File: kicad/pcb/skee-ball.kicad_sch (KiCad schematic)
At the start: 6 parts, among them U1 D24V22F6, U2 MAX98357A, U3 D24V22F5, U4 STM32F091RCTx, U5 74HC595, U6 74HC595

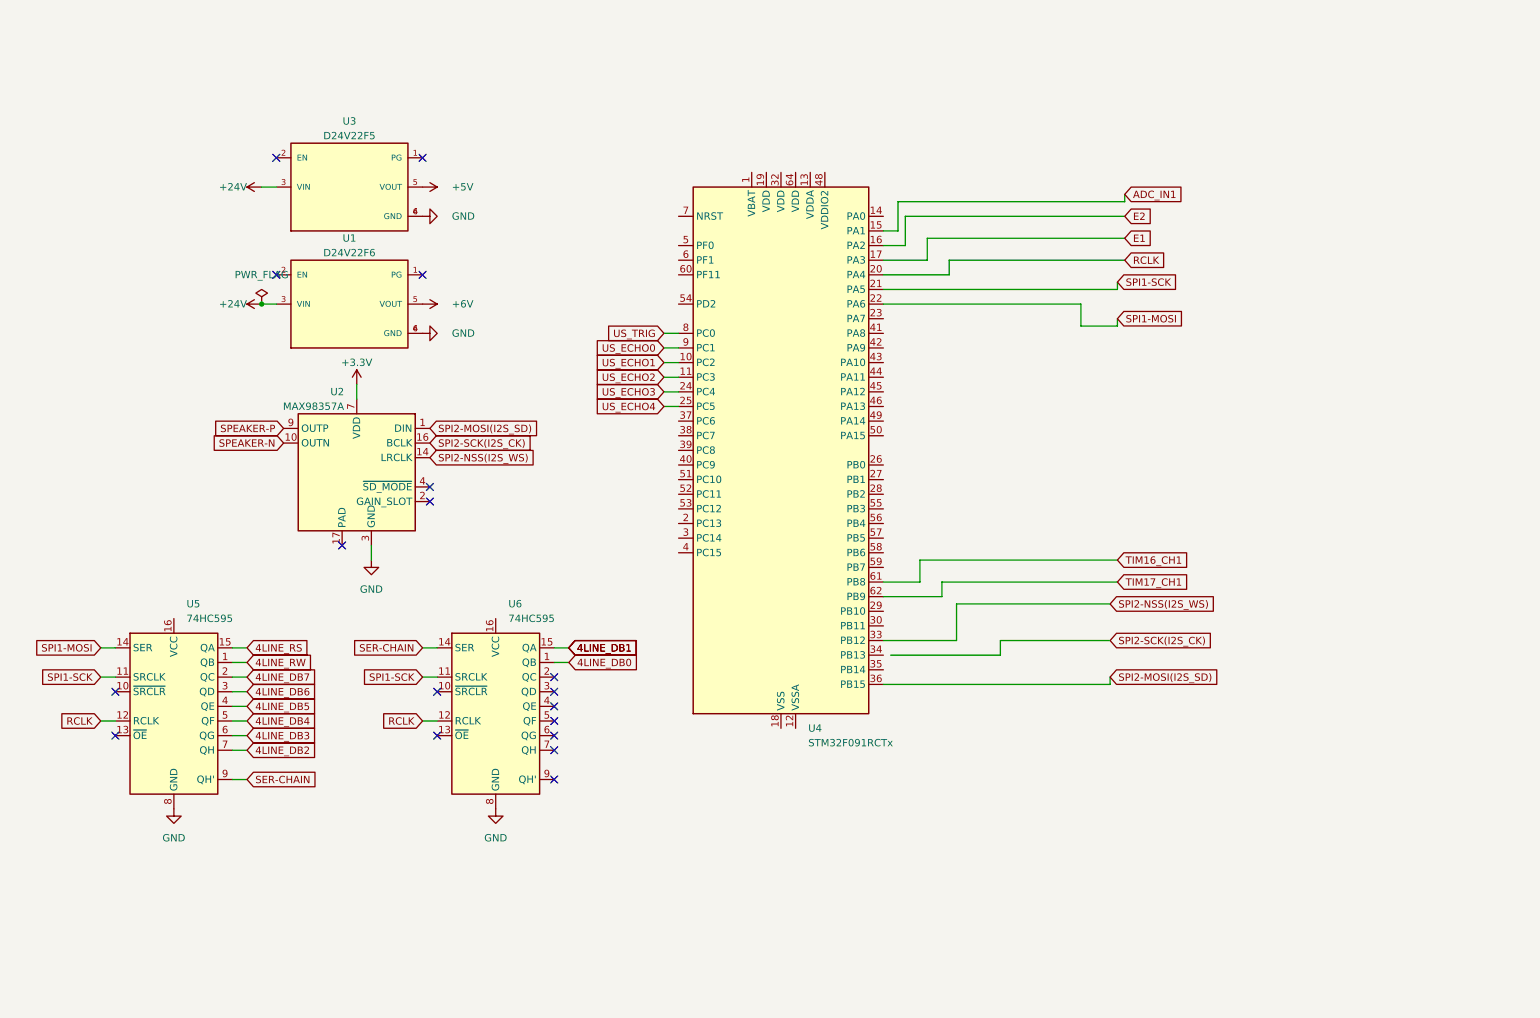
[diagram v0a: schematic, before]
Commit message: add AND gate to pcb schematic
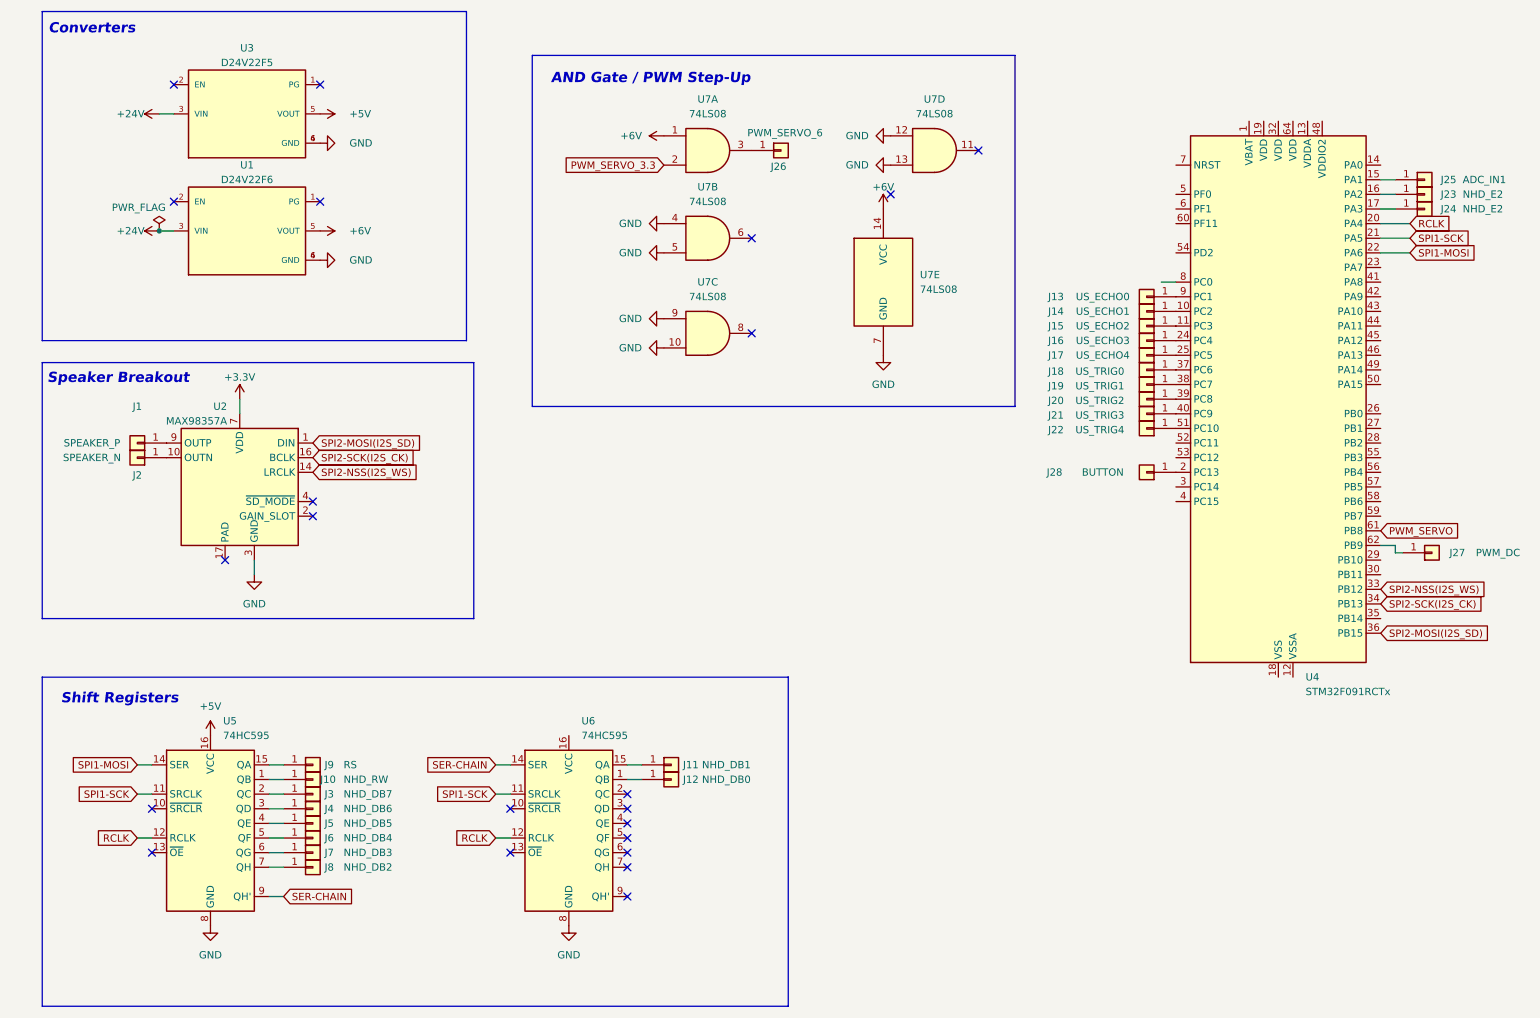
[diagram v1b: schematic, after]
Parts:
- added J1: SPEAKER_P, symbol Connector_Generic:Conn_01x01
- added J10: NHD_RW, symbol Connector_Generic:Conn_01x01
- added J11: NHD_DB1, symbol Connector_Generic:Conn_01x01
- added J12: NHD_DB0, symbol Connector_Generic:Conn_01x01
- added J13: US_ECHO0, symbol Connector_Generic:Conn_01x01
- added J14: US_ECHO1, symbol Connector_Generic:Conn_01x01
- added J15: US_ECHO2, symbol Connector_Generic:Conn_01x01
- added J16: US_ECHO3, symbol Connector_Generic:Conn_01x01
- added J17: US_ECHO4, symbol Connector_Generic:Conn_01x01
- added J18: US_TRIG0, symbol Connector_Generic:Conn_01x01
- added J19: US_TRIG1, symbol Connector_Generic:Conn_01x01
- added J2: SPEAKER_N, symbol Connector_Generic:Conn_01x01
- added J20: US_TRIG2, symbol Connector_Generic:Conn_01x01
- added J21: US_TRIG3, symbol Connector_Generic:Conn_01x01
- added J22: US_TRIG4, symbol Connector_Generic:Conn_01x01
- added J23, J24: NHD_E2, symbol Connector_Generic:Conn_01x01
- added J25: ADC_IN1, symbol Connector_Generic:Conn_01x01
- added J26: PWM_SERVO_6, symbol Connector_Generic:Conn_01x01
- added J27: PWM_DC, symbol Connector_Generic:Conn_01x01
- added J28: BUTTON, symbol Connector_Generic:Conn_01x01
- added J3: NHD_DB7, symbol Connector_Generic:Conn_01x01
- added J4: NHD_DB6, symbol Connector_Generic:Conn_01x01
- added J5: NHD_DB5, symbol Connector_Generic:Conn_01x01
- added J6: NHD_DB4, symbol Connector_Generic:Conn_01x01
- added J7: NHD_DB3, symbol Connector_Generic:Conn_01x01
- added J8: NHD_DB2, symbol Connector_Generic:Conn_01x01
- added J9: RS, symbol Connector_Generic:Conn_01x01
- added U7: 74LS08, symbol 74xx:74LS08
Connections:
- net +5V: now also U5.16 (VCC)
- net +6V: now also U7.1, U7.14 (VCC)
- net GND: now also U7.10, U7.12, U7.13, U7.4, U7.5, U7.7 (GND), U7.9
- net SPI2-SCK(I2S_CK): now also U4.34 (PB13)
- net at U4.2 (PC13): now also J28.1 (Pin_1)
- net at U4.37 (PC6): now also J18.1 (Pin_1)
- net at U4.38 (PC7): now also J19.1 (Pin_1)
- net at U4.39 (PC8): now also J20.1 (Pin_1)
- net at U4.40 (PC9): now also J21.1 (Pin_1)
- net at U4.51 (PC10): now also J22.1 (Pin_1)
- net 4LINE_DB0: no longer names the net of U6.1 (QB)
- net 4LINE_DB0: now also J12.1 (Pin_1)
- net 4LINE_DB1: no longer names the net of U6.15 (QA)
- net 4LINE_DB1: now also J11.1 (Pin_1)
- net 4LINE_DB2: no longer names the net of U5.7 (QH)
- net 4LINE_DB2: now also J8.1 (Pin_1)
- net 4LINE_DB3: no longer names the net of U5.6 (QG)
- net 4LINE_DB3: now also J7.1 (Pin_1)
- net 4LINE_DB4: no longer names the net of U5.5 (QF)
- net 4LINE_DB4: now also J6.1 (Pin_1)
- net 4LINE_DB5: no longer names the net of U5.4 (QE)
- net 4LINE_DB5: now also J5.1 (Pin_1)
- net 4LINE_DB6: no longer names the net of U5.3 (QD)
- net 4LINE_DB6: now also J4.1 (Pin_1)
- net 4LINE_DB7: no longer names the net of U5.2 (QC)
- net 4LINE_DB7: now also J3.1 (Pin_1)
- net 4LINE_RS: no longer names the net of U5.15 (QA)
- net 4LINE_RS: now also J9.1 (Pin_1)
- net 4LINE_RW: no longer names the net of U5.1 (QB)
- net 4LINE_RW: now also J10.1 (Pin_1)
- net ADC_IN1: no longer names the net of U4.15 (PA1)
- net ADC_IN1: now also J25.1 (Pin_1)
- net E1: no longer names the net of U4.17 (PA3)
- net E1: now also J24.1 (Pin_1)
- net E2: no longer names the net of U4.16 (PA2)
- net E2: now also J23.1 (Pin_1)
- net SPEAKER-N: no longer names the net of U2.10 (OUTN)
- net SPEAKER-N: now also J2.1 (Pin_1)
- net SPEAKER-P: no longer names the net of U2.9 (OUTP)
- net SPEAKER-P: now also J1.1 (Pin_1)
- net TIM16_CH1 renamed PWM_SERVO
- net TIM17_CH1: no longer names the net of U4.62 (PB9)
- net TIM17_CH1: now also J27.1 (Pin_1)
- net US_ECHO0: no longer names the net of U4.9 (PC1)
- net US_ECHO0: now also J13.1 (Pin_1)
- net US_ECHO1: no longer names the net of U4.10 (PC2)
- net US_ECHO1: now also J14.1 (Pin_1)
- net US_ECHO2: no longer names the net of U4.11 (PC3)
- net US_ECHO2: now also J15.1 (Pin_1)
- net US_ECHO3: no longer names the net of U4.24 (PC4)
- net US_ECHO3: now also J16.1 (Pin_1)
- net US_ECHO4: no longer names the net of U4.25 (PC5)
- net US_ECHO4: now also J17.1 (Pin_1)
- net US_TRIG: no longer names the net of U4.8 (PC0)
- new net: J26.1 (Pin_1), U7.3
- new net PWM_SERVO_3.3: U7.2
- no-connect marks 18 -> 22
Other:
- note added: "AND Gate / PWM Step-Up"
- note added: "Converters"
- note added: "Shift Registers"
- note added: "Speaker Breakout"
- company: (none) -> Team 1
- title: (none) -> Electronic Skee Ball PCB
- moved on the sheet: U1, U2, U3, U4, U5, U6

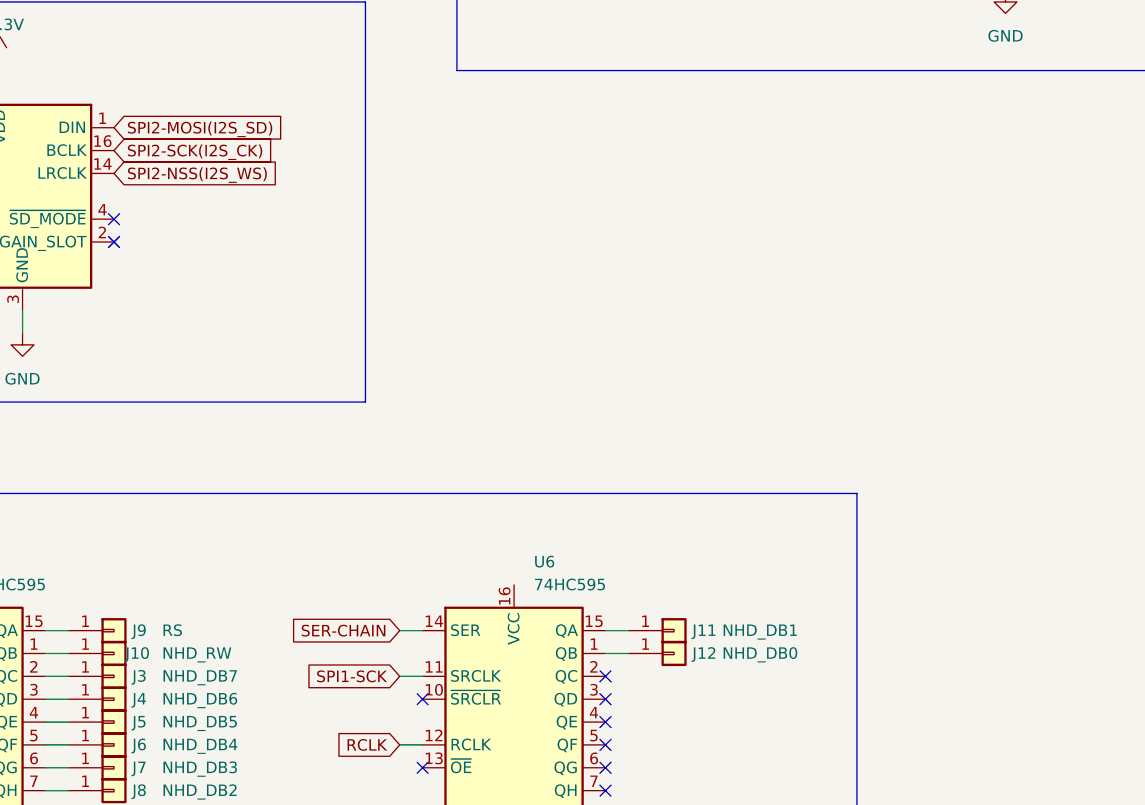
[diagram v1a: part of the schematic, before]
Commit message: add ultrasonic, speaker, nhd
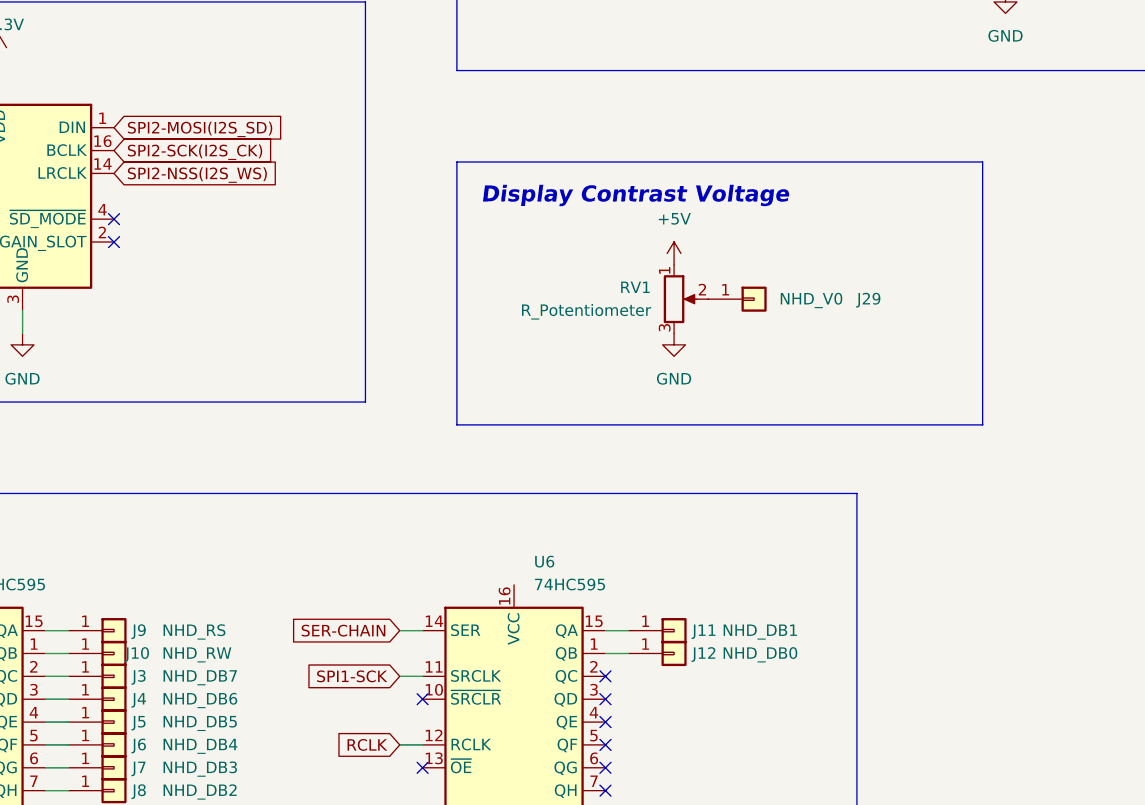
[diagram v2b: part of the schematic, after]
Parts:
- added J29: NHD_V0, symbol Connector_Generic:Conn_01x01
- added RV1: R_Potentiometer, symbol Device:R_Potentiometer
- J9: value RS -> NHD_RS
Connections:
- net +5V: now also RV1.1
- net GND: now also RV1.3
- new net: J29.1 (Pin_1), RV1.2
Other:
- note added: "Display Contrast Voltage"

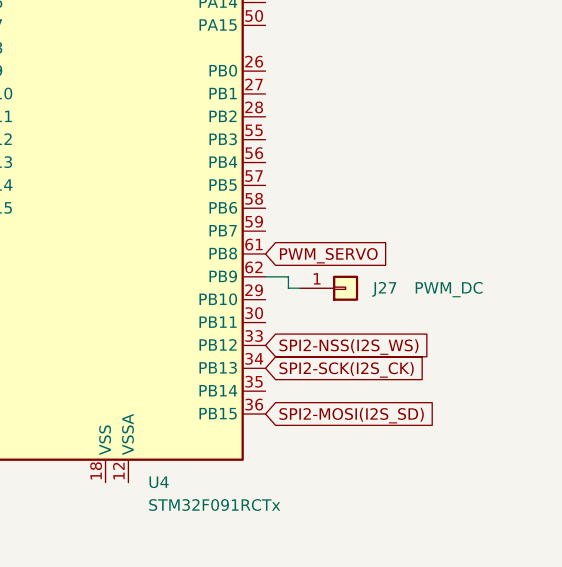
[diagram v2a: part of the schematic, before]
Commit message: add timer labels to pwm signals
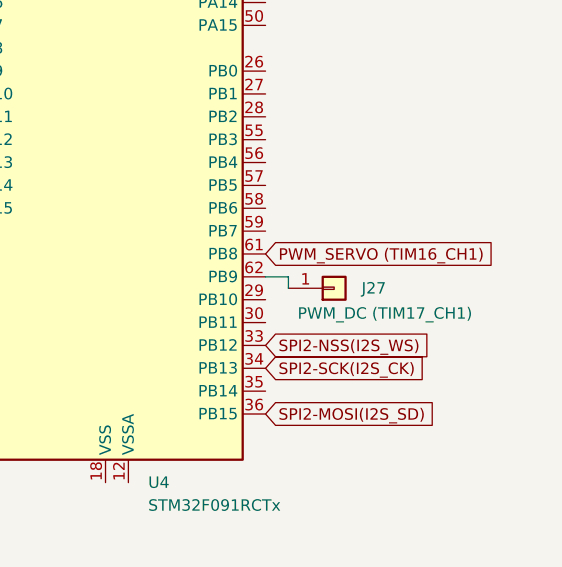
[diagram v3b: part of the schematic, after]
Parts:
- J27: value PWM_DC -> PWM_DC (TIM17_CH1)
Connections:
- net PWM_SERVO renamed PWM_SERVO (TIM16_CH1)
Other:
- moved on the sheet: J27
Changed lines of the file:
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@@
-	(wire
-		(pts
-			(xy 256.54 114.3) (xy 257.81 114.3)
-		)
-		(stroke
-			(width 0)
-			(type default)
-		)
-	)
 	(wire
 		(pts
@@
 		)
 	)
-	(global_label "PWM_SERVO"
+	(global_label "PWM_SERVO (TIM16_CH1)"
 		(shape input)
 		(at 254 110.49 0)
@@
 		)
 		(property "Intersheetrefs" "${INTERSHEET_REFS}"
-			(at 268.6492 110.49 0)
+			(at 281.0546 110.49 0)
 			(effects
 				(font
@@
 	(symbol
 		(lib_id "Connector_Generic:Conn_01x01")
-		(at 262.89 114.3 0)
+		(at 261.62 114.3 0)
 		(mirror x)
 		(unit 1)
@@
 		(dnp no)
 		(property "Reference" "J27"
-			(at 265.938 114.3 0)
-			(effects
-				(font
-					(size 1.27 1.27)
-				)
-				(justify left)
-			)
-		)
-		(property "Value" "PWM_DC"
-			(at 270.51 114.3 0)
+			(at 264.668 114.3 0)
+			(effects
+				(font
+					(size 1.27 1.27)
+				)
+				(justify left)
+			)
+		)
+		(property "Value" "PWM_DC (TIM17_CH1)"
+			(at 257.556 117.094 0)
 			(effects
 				(font
@@
 		)
 		(property "Footprint" ""
-			(at 262.89 114.3 0)
+			(at 261.62 114.3 0)
 			(effects
 				(font
@@
 		)
 		(property "Datasheet" "~"
-			(at 262.89 114.3 0)
+			(at 261.62 114.3 0)
 			(effects
 				(font
@@
 		)
 		(property "Description" "Generic connector, single row, 01x01, script generated (kicad-library-utils/schlib/autogen/connector/)"
-			(at 262.89 114.3 0)
-			(effects
-				(font
+			(at 261.62 114.3 0)
+			(effects
+				(font

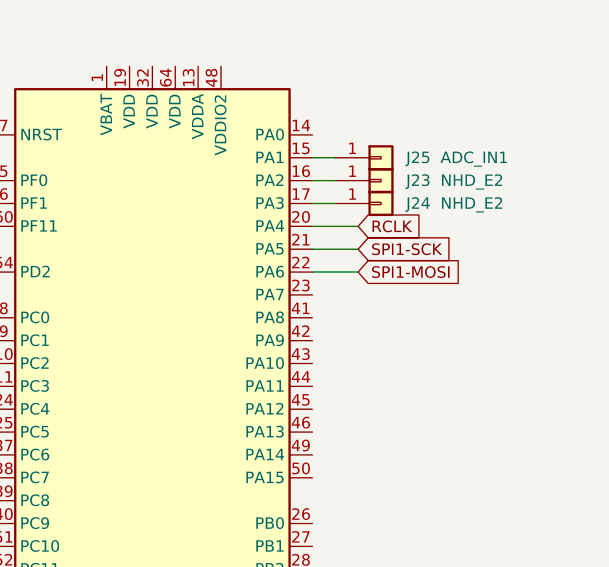
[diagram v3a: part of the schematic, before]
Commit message: fix spi1 mosi pin assignment
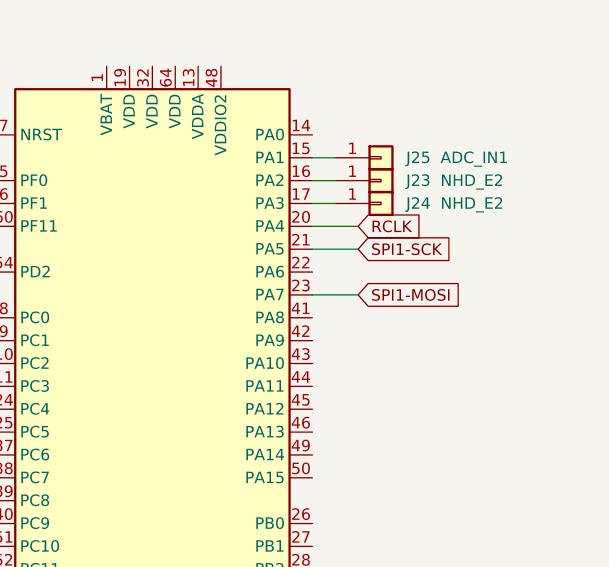
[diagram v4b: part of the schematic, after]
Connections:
- net SPI1-MOSI: now also U4.23 (PA7); no longer U4.22 (PA6)
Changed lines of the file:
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@@
+	(wire
+		(pts
+			(xy 254 64.77) (xy 259.08 64.77)
+		)
+		(stroke
+			(width 0)
+			(type default)
+		)
+	)
 	(wire
 		(pts
@@
 		(pts
 			(xy 38.1 163.83) (xy 40.64 163.83)
-		)
-		(stroke
-			(width 0)
-			(type default)
-		)
-	)
-	(wire
-		(pts
-			(xy 254 62.23) (xy 259.08 62.23)
 		)
 		(stroke
@@
 	(global_label "SPI1-MOSI"
 		(shape input)
-		(at 259.08 62.23 0)
+		(at 259.08 64.77 0)
 		(fields_autoplaced yes)
 		(effects
@@
 		)
 		(property "Intersheetrefs" "${INTERSHEET_REFS}"
-			(at 272.5276 62.23 0)
+			(at 272.5276 64.77 0)
 			(effects
 				(font
